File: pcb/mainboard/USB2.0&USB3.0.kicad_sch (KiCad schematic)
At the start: 25 parts, among them J79 USB3_A, J80 USB3_A, J81 USB_C_Receptacle_USB2.0_16P, J82 Conn_01x03_Pin, U3 ULC0524P, U4 ULC0524P, U5 ULC0524P

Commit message: before i start jul 10th
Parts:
- removed J82: Conn_01x03_Pin, Connector_PinSocket_2.54mm:PinSocket_1x03_P2.54mm_Vertical, symbol Connector:Conn_01x03_Pin
- added J82: Conn_01x04_Pin, Connector_PinHeader_2.54mm:PinHeader_1x04_P2.54mm_Vertical, symbol Connector:Conn_01x04_Pin
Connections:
- net GND: now also J82.4 (Pin_4)
- net USB_2_P3+: now also J82.2 (Pin_2)
- net USB_2_P3-: now also J82.3 (Pin_3)
- net at F78.2: now also J82.1 (Pin_1)
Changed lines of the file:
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@@
 	(wire
 		(pts
-			(xy 328.93 105.41) (xy 328.93 128.27)
-		)
-		(stroke
-			(width 0)
-			(type default)
-		)
-	)
-	(wire
-		(pts
 			(xy 344.17 95.25) (xy 355.6 95.25)
 		)
@@
 	(wire
 		(pts
+			(xy 328.93 134.62) (xy 345.44 134.62)
+		)
+		(stroke
+			(width 0)
+			(type default)
+		)
+	)
+	(wire
+		(pts
 			(xy 245.11 194.31) (xy 313.69 194.31)
 		)
@@
 	(wire
 		(pts
+			(xy 328.93 105.41) (xy 328.93 134.62)
+		)
+		(stroke
+			(width 0)
+			(type default)
+		)
+	)
+	(wire
+		(pts
 			(xy 373.38 133.35) (xy 373.38 137.16)
 		)
@@
 	)
 	(symbol
-		(lib_id "Connector:Conn_01x03_Pin")
-		(at 350.52 139.7 0)
-		(mirror y)
-		(unit 1)
-		(exclude_from_sim no)
-		(in_bom yes)
-		(on_board yes)
-		(dnp no)
-		(fields_autoplaced yes)
-		(property "Reference" "J82"
-			(at 351.79 138.4299 0)
-			(effects
-				(font
-					(size 1.27 1.27)
-				)
-				(justify right)
-			)
-		)
-		(property "Value" "Conn_01x03_Pin"
-			(at 351.79 140.9699 0)
-			(effects
-				(font
-					(size 1.27 1.27)
-				)
-				(justify right)
-			)
-		)
-		(property "Footprint" "Connector_PinSocket_2.54mm:PinSocket_1x03_P2.54mm_Vertical"
-			(at 350.52 139.7 0)
-			(effects
-				(font
-					(size 1.27 1.27)
-				)
-				(hide yes)
-			)
-		)
-		(property "Datasheet" "~"
-			(at 350.52 139.7 0)
-			(effects
-				(font
-					(size 1.27 1.27)
-				)
-				(hide yes)
-			)
-		)
-		(property "Description" "Generic connector, single row, 01x03, script generated"
-			(at 350.52 139.7 0)
-			(effects
-				(font
-					(size 1.27 1.27)
-				)
-				(hide yes)
-			)
-		)
-		(pin "1"
-		)
-		(pin "2"
-		)
-		(pin "3"
-		)
-		(instances
-			(project ""
-				(path "/2a6d114a-7fd7-4207-b5f7-4ea9c34f36aa/f9aa04f2-8362-4e9f-9e54-e2b1a8ec9b0a"
-					(reference "J82")
-					(unit 1)
-				)
-			)
-		)
-	)
-	(symbol
 		(lib_id "Power_Protection:D3V3XA4B10LP")
 		(at 248.92 231.14 0)
@@
 					(unit 1)
 				)
+			)
+		)
+	)
+	(symbol
+		(lib_id "Connector:Conn_01x04_Pin")
+		(at 350.52 137.16 0)
+		(mirror y)
+		(unit 1)
+		(exclude_from_sim no)
+		(in_bom yes)
+		(on_board yes)
+		(dnp no)
+		(fields_autoplaced yes)
+		(property "Reference" "J82"
+			(at 351.79 137.1599 0)
+			(effects
+				(font
+					(size 1.27 1.27)
+				)
+				(justify right)
+			)
+		)
+		(property "Value" "Conn_01x04_Pin"
+			(at 351.79 139.6999 0)
+			(effects
+				(font
+					(size 1.27 1.27)
+				)
+				(justify right)
+			)
+		)
+		(property "Footprint" "Connector_PinHeader_2.54mm:PinHeader_1x04_P2.54mm_Vertical"
+			(at 350.52 137.16 0)
+			(effects
+				(font
+					(size 1.27 1.27)
+				)
+				(hide yes)
+			)
+		)
+		(property "Datasheet" "~"
+			(at 350.52 137.16 0)
+			(effects
+				(font
+					(size 1.27 1.27)
+				)
+				(hide yes)
+			)
+		)
+		(property "Description" "Generic connector, single row, 01x04, script generated"
+			(at 350.52 137.16 0)
+			(effects
+				(font
+					(size 1.27 1.27)
+				)
+				(hide yes)
+			)
+		)
+		(pin "1"
+		)
+		(pin "2"
+		)
+		(pin "4"
+		)
+		(pin "3"
+		)
+		(instances
+			(project ""
+				(path "/2a6d114a-7fd7-4207-b5f7-4ea9c34f36aa/f9aa04f2-8362-4e9f-9e54-e2b1a8ec9b0a"
+					(reference "J82")
+					(unit 1)
+				)

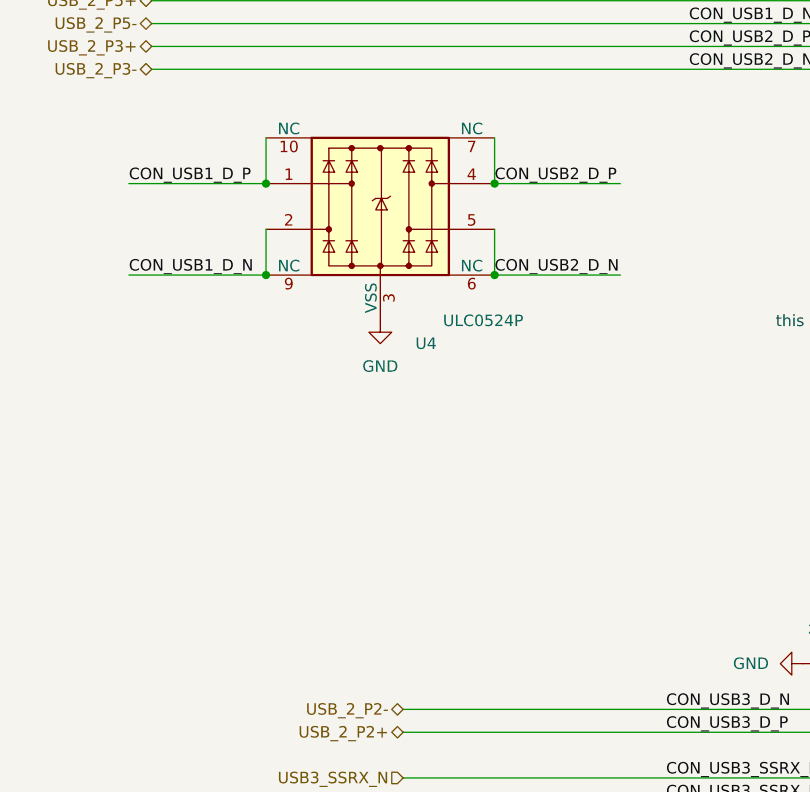
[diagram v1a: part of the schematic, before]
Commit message: added extra esd to schem but not pcb also routed differential pairs of hdmi
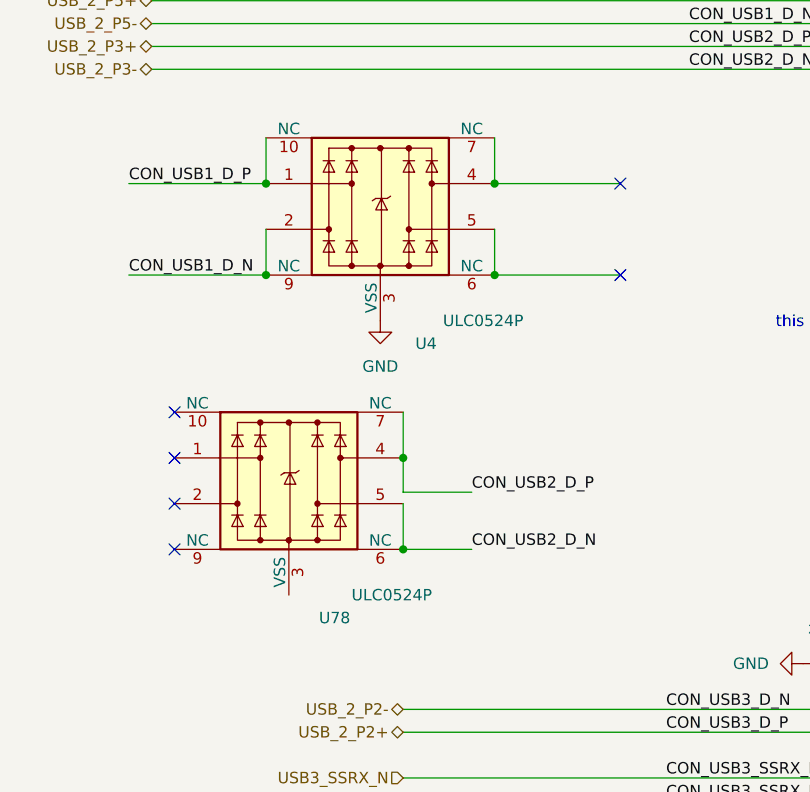
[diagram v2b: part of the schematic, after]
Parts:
- added U78: ULC0524P, A_HDJ_Library:Diodes_UDFN-10_1.0x2.5mm_P0.5mm, symbol Power_Protection:D3V3XA4B10LP
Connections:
- net USB_2_P3+: now also U78.4, U78.7 (NC); no longer U4.4, U4.7 (NC)
- net USB_2_P3-: now also U78.5, U78.6 (NC); no longer U4.5, U4.6 (NC)
- new net: U78.3 (VSS), U78.8 (VSS)
- new net: U4.4, U4.7 (NC)
- new net: U4.5, U4.6 (NC)
- no-connect marks 2 -> 8
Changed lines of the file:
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@@
+	)
+	(junction
+		(at 245.11 168.91)
+		(diameter 0)
+		(color 0 0 0 0)
 	)
 	(junction
@@
 	)
 	(junction
+		(at 245.11 158.75)
+		(diameter 0)
+		(color 0 0 0 0)
+	)
+	(junction
 		(at 331.47 228.6)
 		(diameter 0)
@@
 	)
 	(no_connect
+		(at 219.71 158.75)
+	)
+	(no_connect
 		(at 355.6 125.73)
+	)
+	(no_connect
+		(at 219.71 168.91)
+	)
+	(no_connect
+		(at 219.71 153.67)
 	)
 	(no_connect
 		(at 355.6 123.19)
 	)
+	(no_connect
+		(at 269.24 128.27)
+	)
+	(no_connect
+		(at 219.71 163.83)
+	)
+	(no_connect
+		(at 269.24 138.43)
+	)
 	(wire
 		(pts
@@
 	(wire
 		(pts
+			(xy 245.11 168.91) (xy 252.73 168.91)
+		)
+		(stroke
+			(width 0)
+			(type default)
+		)
+	)
+	(wire
+		(pts
 			(xy 354.33 102.87) (xy 355.6 102.87)
 		)
@@
 	(wire
 		(pts
+			(xy 245.11 163.83) (xy 245.11 168.91)
+		)
+		(stroke
+			(width 0)
+			(type default)
+		)
+	)
+	(wire
+		(pts
 			(xy 217.17 115.57) (xy 318.77 115.57)
 		)
@@
 	(wire
 		(pts
+			(xy 245.11 153.67) (xy 245.11 158.75)
+		)
+		(stroke
+			(width 0)
+			(type default)
+		)
+	)
+	(wire
+		(pts
 			(xy 184.15 257.81) (xy 184.15 266.7)
 		)
@@
 	(wire
 		(pts
+			(xy 245.11 162.56) (xy 245.11 158.75)
+		)
+		(stroke
+			(width 0)
+			(type default)
+		)
+	)
+	(wire
+		(pts
 			(xy 163.83 231.14) (xy 207.01 231.14)
 		)
@@
 		(pts
 			(xy 173.99 266.7) (xy 184.15 266.7)
+		)
+		(stroke
+			(width 0)
+			(type default)
+		)
+	)
+	(wire
+		(pts
+			(xy 252.73 162.56) (xy 245.11 162.56)
 		)
 		(stroke
@@
 	)
 	(label "CON_USB2_D_N"
-		(at 255.27 138.43 0)
+		(at 252.73 168.91 0)
 		(effects
 			(font
@@
 		)
 	)
+	(label "CON_USB2_D_P"
+		(at 252.73 162.56 0)
+		(effects
+			(font
+				(size 1.27 1.27)
+			)
+			(justify left bottom)
+		)
+	)
 	(label "CON_USB4_D_P"
 		(at 274.32 267.97 0)
@@
 	(label "CON_USB4_SSRX_P"
 		(at 287.02 238.76 0)
-		(effects
-			(font
-				(size 1.27 1.27)
-			)
-			(justify left bottom)
-		)
-	)
-	(label "CON_USB2_D_P"
-		(at 255.27 128.27 0)
 		(effects
 			(font
@@
 					(unit 1)
 				)
+			)
+		)
+	)
+	(symbol
+		(lib_id "Power_Protection:D3V3XA4B10LP")
+		(at 232.41 161.29 0)
+		(unit 1)
+		(exclude_from_sim no)
+		(in_bom yes)
+		(on_board yes)
+		(dnp no)
+		(property "Reference" "U78"
+			(at 237.49 176.53 0)
+			(effects
+				(font
+					(size 1.27 1.27)
+				)
+			)
+		)
+		(property "Value" "ULC0524P"
+			(at 243.84 173.99 0)
+			(effects
+				(font
+					(size 1.27 1.27)
+				)
+			)
+		)
+		(property "Footprint" "A_HDJ_Library:Diodes_UDFN-10_1.0x2.5mm_P0.5mm"
+			(at 208.28 171.45 0)
+			(effects
+				(font
+					(size 1.27 1.27)
+				)
+				(hide yes)
+			)
+		)
+		(property "Datasheet" "https://www.diodes.com/assets/Datasheets/D3V3XA4B10LP.pdf"
+			(at 232.41 161.29 0)
+			(effects
+				(font
+					(size 1.27 1.27)
+				)
+				(hide yes)
+			)
+		)
+		(property "Description" ""
+			(at 232.41 161.29 0)
+			(effects
+				(font
+					(size 1.27 1.27)
+				)
+				(hide yes)
+			)
+		)
+		(property "SCH_Show_Footprint" ""
+			(at 232.41 161.29 0)
+			(effects
+				(font
+					(size 1.27 1.27)
+				)
+				(hide yes)
+			)
+		)
+		(property "Sim.Device" ""
+			(at 232.41 161.29 0)
+			(effects
+				(font
+					(size 1.27 1.27)
+				)
+				(hide yes)
+			)
+		)
+		(property "Sim.Pins" ""
+			(at 232.41 161.29 0)
+			(effects
+				(font
+					(size 1.27 1.27)
+				)
+				(hide yes)
+			)
+		)
+		(property "Sim.Type" ""
+			(at 232.41 161.29 0)
+			(effects
+				(font
+					(size 1.27 1.27)
+				)
+				(hide yes)
+			)
+		)
+		(pin "2"
+		)
+		(pin "6"
+		)
+		(pin "1"
+		)
+		(pin "7"
+		)
+		(pin "8"
+		)
+		(pin "3"
+		)
+		(pin "5"
+		)
+		(pin "4"
+		)
+		(pin "10"
+		)
+		(pin "9"
+		)
+		(instances
+			(project "[DFR1142]Lite Carrier for LattePanda Mu"
+				(path "/2a6d114a-7fd7-4207-b5f7-4ea9c34f36aa/f9aa04f2-8362-4e9f-9e54-e2b1a8ec9b0a"
+					(reference "U78")
+					(unit 1)
+				)

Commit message: gtg leave
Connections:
- net CON_USB3_SSTX_N: now also U3.5, U3.6 (NC); no longer U3.4, U3.7 (NC)
- net CON_USB3_SSTX_P: now also U3.4, U3.7 (NC); no longer U3.5, U3.6 (NC)
- net CON_USB4_SSTX_N: now also U5.4, U5.7 (NC); no longer U3.1, U3.10 (NC)
- net CON_USB4_SSTX_P: now also U5.5, U5.6 (NC); no longer U3.2, U3.9 (NC)
- net USB3_SSRX_N: now also U3.2, U3.9 (NC); no longer U5.4, U5.7 (NC)
- net USB3_SSRX_P: now also U3.1, U3.10 (NC); no longer U5.5, U5.6 (NC)
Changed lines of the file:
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@@
+	)
+	(junction
+		(at 236.22 236.22)
+		(diameter 0)
+		(color 0 0 0 0)
 	)
 	(junction
@@
 	)
 	(junction
-		(at 236.22 228.6)
-		(diameter 0)
-		(color 0 0 0 0)
-	)
-	(junction
 		(at 184.15 266.7)
 		(diameter 0)
@@
 	)
 	(junction
+		(at 331.47 228.6)
+		(diameter 0)
+		(color 0 0 0 0)
+	)
+	(junction
 		(at 245.11 168.91)
 		(diameter 0)
@@
 	)
 	(junction
+		(at 236.22 227.33)
+		(diameter 0)
+		(color 0 0 0 0)
+	)
+	(junction
 		(at 344.17 100.33)
 		(diameter 0)
@@
 	)
 	(junction
-		(at 331.47 238.76)
-		(diameter 0)
-		(color 0 0 0 0)
-	)
-	(junction
 		(at 297.18 105.41)
 		(diameter 0)
@@
 	)
 	(junction
-		(at 331.47 228.6)
-		(diameter 0)
-		(color 0 0 0 0)
-	)
-	(junction
 		(at 306.07 238.76)
 		(diameter 0)
@@
 	)
 	(junction
+		(at 331.47 237.49)
+		(diameter 0)
+		(color 0 0 0 0)
+	)
+	(junction
 		(at 306.07 228.6)
 		(diameter 0)
@@
 	(junction
 		(at 289.56 100.33)
-		(diameter 0)
-		(color 0 0 0 0)
-	)
-	(junction
-		(at 236.22 238.76)
 		(diameter 0)
 		(color 0 0 0 0)
@@
 	(wire
 		(pts
+			(xy 331.47 233.68) (xy 331.47 237.49)
+		)
+		(stroke
+			(width 0)
+			(type default)
+		)
+	)
+	(wire
+		(pts
 			(xy 217.17 107.95) (xy 345.44 107.95)
 		)
@@
 	(wire
 		(pts
-			(xy 331.47 238.76) (xy 349.25 238.76)
-		)
-		(stroke
-			(width 0)
-			(type default)
-		)
-	)
-	(wire
-		(pts
 			(xy 321.31 113.03) (xy 321.31 137.16)
 		)
@@
 	(wire
 		(pts
+			(xy 215.9 227.33) (xy 236.22 227.33)
+		)
+		(stroke
+			(width 0)
+			(type default)
+		)
+	)
+	(wire
+		(pts
+			(xy 215.9 236.22) (xy 236.22 236.22)
+		)
+		(stroke
+			(width 0)
+			(type default)
+		)
+	)
+	(wire
+		(pts
 			(xy 245.11 280.67) (xy 252.73 280.67)
 		)
@@
 	(wire
 		(pts
-			(xy 215.9 238.76) (xy 236.22 238.76)
-		)
-		(stroke
-			(width 0)
-			(type default)
-		)
-	)
-	(wire
-		(pts
 			(xy 326.39 288.29) (xy 328.93 288.29)
 		)
@@
 	(wire
 		(pts
+			(xy 331.47 223.52) (xy 331.47 228.6)
+		)
+		(stroke
+			(width 0)
+			(type default)
+		)
+	)
+	(wire
+		(pts
 			(xy 184.15 236.22) (xy 184.15 250.19)
 		)
@@
 	(wire
 		(pts
+			(xy 340.36 229.87) (xy 331.47 229.87)
+		)
+		(stroke
+			(width 0)
+			(type default)
+		)
+	)
+	(wire
+		(pts
 			(xy 245.11 163.83) (xy 245.11 168.91)
 		)
@@
 	(wire
 		(pts
+			(xy 236.22 223.52) (xy 236.22 227.33)
+		)
+		(stroke
+			(width 0)
+			(type default)
+		)
+	)
+	(wire
+		(pts
 			(xy 245.11 189.23) (xy 313.69 189.23)
 		)
@@
 	(wire
 		(pts
-			(xy 331.47 228.6) (xy 349.25 228.6)
-		)
-		(stroke
-			(width 0)
-			(type default)
-		)
-	)
-	(wire
-		(pts
 			(xy 326.39 100.33) (xy 326.39 95.25)
 		)
@@
 	(wire
 		(pts
-			(xy 331.47 233.68) (xy 331.47 238.76)
+			(xy 215.9 236.22) (xy 215.9 238.76)
 		)
 		(stroke
@@
 	(wire
 		(pts
-			(xy 331.47 223.52) (xy 331.47 228.6)
+			(xy 215.9 227.33) (xy 215.9 228.6)
+		)
+		(stroke
+			(width 0)
+			(type default)
+		)
+	)
+	(wire
+		(pts
+			(xy 331.47 229.87) (xy 331.47 228.6)
 		)
 		(stroke
@@
 	(wire
 		(pts
-			(xy 236.22 223.52) (xy 236.22 228.6)
-		)
-		(stroke
-			(width 0)
-			(type default)
-		)
-	)
-	(wire
-		(pts
 			(xy 245.11 283.21) (xy 252.73 283.21)
 		)
@@
 	(wire
 		(pts
-			(xy 215.9 228.6) (xy 236.22 228.6)
+			(xy 339.09 228.6) (xy 340.36 228.6)
 		)
 		(stroke
@@
 	(wire
 		(pts
+			(xy 236.22 227.33) (xy 236.22 228.6)
+		)
+		(stroke
+			(width 0)
+			(type default)
+		)
+	)
+	(wire
+		(pts
 			(xy 261.62 228.6) (xy 280.67 228.6)
 		)
@@
 	(wire
 		(pts
+			(xy 331.47 237.49) (xy 331.47 238.76)
+		)
+		(stroke
+			(width 0)
+			(type default)
+		)
+	)
+	(wire
+		(pts
 			(xy 328.93 105.41) (xy 328.93 134.62)
 		)
@@
 	(wire
 		(pts
+			(xy 339.09 237.49) (xy 331.47 237.49)
+		)
+		(stroke
+			(width 0)
+			(type default)
+		)
+	)
+	(wire
+		(pts
 			(xy 302.26 260.35) (xy 297.18 260.35)
 		)
@@
 	(wire
 		(pts
+			(xy 340.36 228.6) (xy 340.36 229.87)
+		)
+		(stroke
+			(width 0)
+			(type default)
+		)
+	)
+	(wire
+		(pts
 			(xy 245.11 267.97) (xy 313.69 267.97)
 		)
@@
 	(wire
 		(pts
-			(xy 236.22 233.68) (xy 236.22 238.76)
+			(xy 236.22 233.68) (xy 236.22 236.22)
 		)
 		(stroke
@@
 	(wire
 		(pts
+			(xy 236.22 236.22) (xy 236.22 238.76)
+		)
+		(stroke
+			(width 0)
+			(type default)
+		)
+	)
+	(wire
+		(pts
 			(xy 173.99 266.7) (xy 184.15 266.7)
 		)
@@
 		)
 	)
-	(label "CON_USB3_SSTX_N"
-		(at 261.62 228.6 0)
+	(label "CON_USB3_SSRX_P"
+		(at 215.9 228.6 0)
 		(effects
 			(font
@@
 		)
 	)
-	(label "CON_USB3_SSTX_P"
-		(at 261.62 238.76 0)
-		(effects
-			(font
-				(size 1.27 1.27)
-			)
-			(justify left bottom)
-		)
-	)
 	(label "CON_USB2_D_N"
 		(at 276.86 115.57 0)
@@
 	)
 	(label "CON_USB4_SSTX_P"
-		(at 215.9 238.76 0)
-		(effects
-			(font
-				(size 1.27 1.27)
-			)
-			(justify left bottom)
-		)
-	)
-	(label "CON_USB3_SSRX_N"
-		(at 331.47 228.6 0)
+		(at 339.09 237.49 0)
 		(effects
 			(font
@@
 		)
 	)
+	(label "CON_USB3_SSTX_N"
+		(at 261.62 238.76 0)
+		(effects
+			(font
+				(size 1.27 1.27)
+			)
+			(justify left bottom)
+		)
+	)
 	(label "CON_USB4_SSRX_N"
 		(at 287.02 228.6 0)
@@
 		)
 	)
+	(label "CON_USB3_SSTX_P"
+		(at 261.62 228.6 0)
+		(effects
+			(font
+				(size 1.27 1.27)
+			)
+			(justify left bottom)
+		)
+	)
 	(label "CON_USB4_SSRX_P"
 		(at 274.32 275.59 0)
@@
 	)
 	(label "CON_USB3_SSRX_N"
+		(at 215.9 238.76 0)
+		(effects
+			(font
+				(size 1.27 1.27)
+			)
+			(justify left bottom)
+		)
+	)
+	(label "CON_USB3_SSRX_N"
 		(at 274.32 194.31 0)
 		(effects
@@
 	)
 	(label "CON_USB4_SSTX_N"
-		(at 215.9 228.6 0)
+		(at 339.09 228.6 0)
 		(effects
 			(font
@@
 		(effects
 			(font
-				(size 1.27 1.27)
-			)
-			(justify left bottom)
-		)
-	)
-	(label "CON_USB3_SSRX_P"
-		(at 331.47 238.76 0)
-		(effects
-			(font

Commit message: latest
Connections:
- net CON_USB3_SSTX_N: now also U3.4, U3.7 (NC); no longer U3.5, U3.6 (NC)
- net CON_USB3_SSTX_P: now also U3.5, U3.6 (NC); no longer U3.4, U3.7 (NC)
- net USB3_SSRX_N: now also U3.1, U3.10 (NC); no longer U3.2, U3.9 (NC)
- net USB3_SSRX_P: now also U3.2, U3.9 (NC); no longer U3.1, U3.10 (NC)
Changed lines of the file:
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@@
-		)
-	)
-	(label "CON_USB3_SSRX_P"
-		(at 215.9 228.6 0)
-		(effects
-			(font
-				(size 1.27 1.27)
-			)
-			(justify left bottom)
 		)
 	)
@@
 		)
 	)
+	(label "CON_USB3_SSRX_P"
+		(at 215.9 238.76 0)
+		(effects
+			(font
+				(size 1.27 1.27)
+			)
+			(justify left bottom)
+		)
+	)
 	(label "CON_USB4_D_P"
 		(at 207.01 231.14 180)
@@
 		)
 	)
-	(label "CON_USB3_SSTX_N"
-		(at 261.62 238.76 0)
-		(effects
-			(font
-				(size 1.27 1.27)
-			)
-			(justify left bottom)
-		)
-	)
 	(label "CON_USB4_SSRX_N"
 		(at 287.02 228.6 0)
@@
 		)
 	)
-	(label "CON_USB3_SSTX_P"
-		(at 261.62 228.6 0)
-		(effects
-			(font
-				(size 1.27 1.27)
-			)
-			(justify left bottom)
-		)
-	)
 	(label "CON_USB4_SSRX_P"
 		(at 274.32 275.59 0)
@@
 	)
 	(label "CON_USB3_SSRX_N"
-		(at 215.9 238.76 0)
+		(at 274.32 194.31 0)
 		(effects
 			(font
@@
 	)
 	(label "CON_USB3_SSRX_N"
-		(at 274.32 194.31 0)
+		(at 215.9 228.6 0)
 		(effects
 			(font
@@
 		)
 	)
+	(label "CON_USB3_SSTX_N"
+		(at 261.62 228.6 0)
+		(effects
+			(font
+				(size 1.27 1.27)
+			)
+			(justify left bottom)
+		)
+	)
 	(label "CON_USB3_SSTX_P"
 		(at 274.32 204.47 0)
@@
 		(effects
 			(font
+				(size 1.27 1.27)
+			)
+			(justify left bottom)
+		)
+	)
+	(label "CON_USB3_SSTX_P"
+		(at 261.62 238.76 0)
+		(effects
+			(font
